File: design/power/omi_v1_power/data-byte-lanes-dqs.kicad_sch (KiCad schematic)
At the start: 3 parts

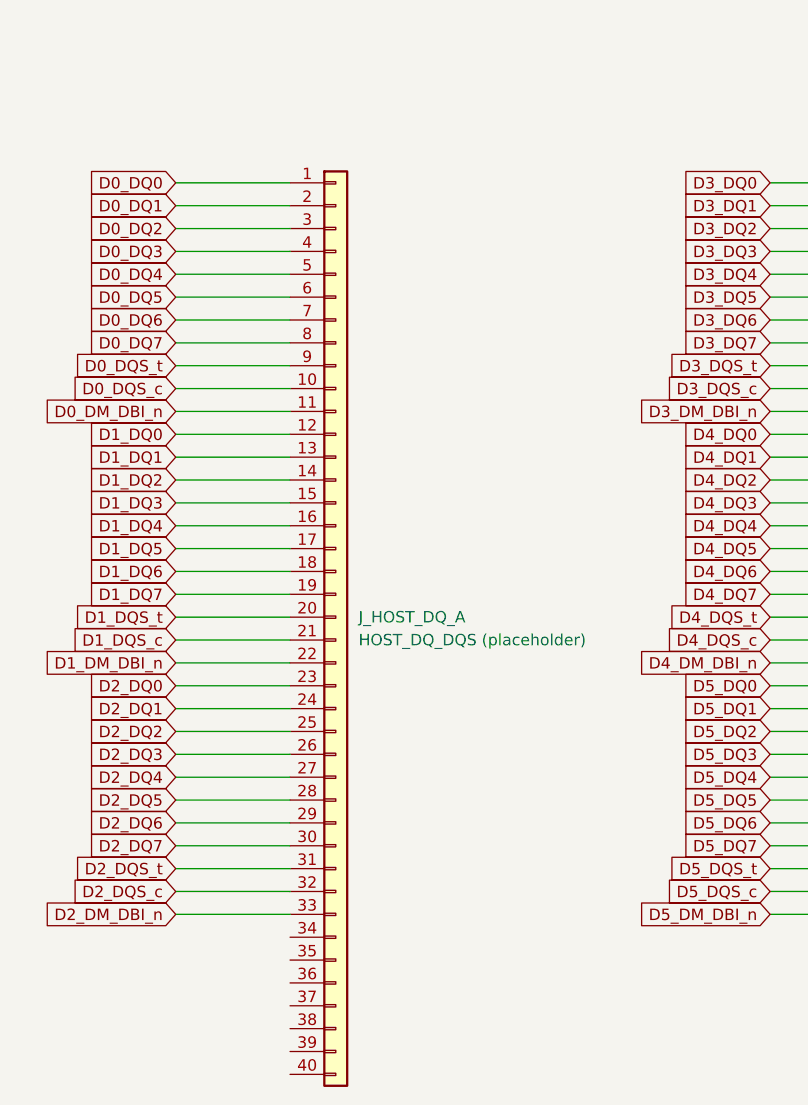
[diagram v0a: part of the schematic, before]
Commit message: feat(phase3): remove redundant J_HOST_DQ_A placeholder (byte lanes D0-D2)
J1 carries every D0/D1/D2 DQ/DQS/DM net; each verified to still hold
{J1, U_DRAMn} after removal (e.g. D0_DQ0 -> {J1, U_DRAM0}). Removed symbol + its
33 pin global labels + 33 wire stubs. J_HOST_DQ_B/C intact (verified: 33/22
labels, nets unchanged). ERC 132 -> 125 (data pin_not_connected 32 -> 25).

Co-Authored-By: Claude Opus 4.8 (1M context) <noreply@anthropic.com>
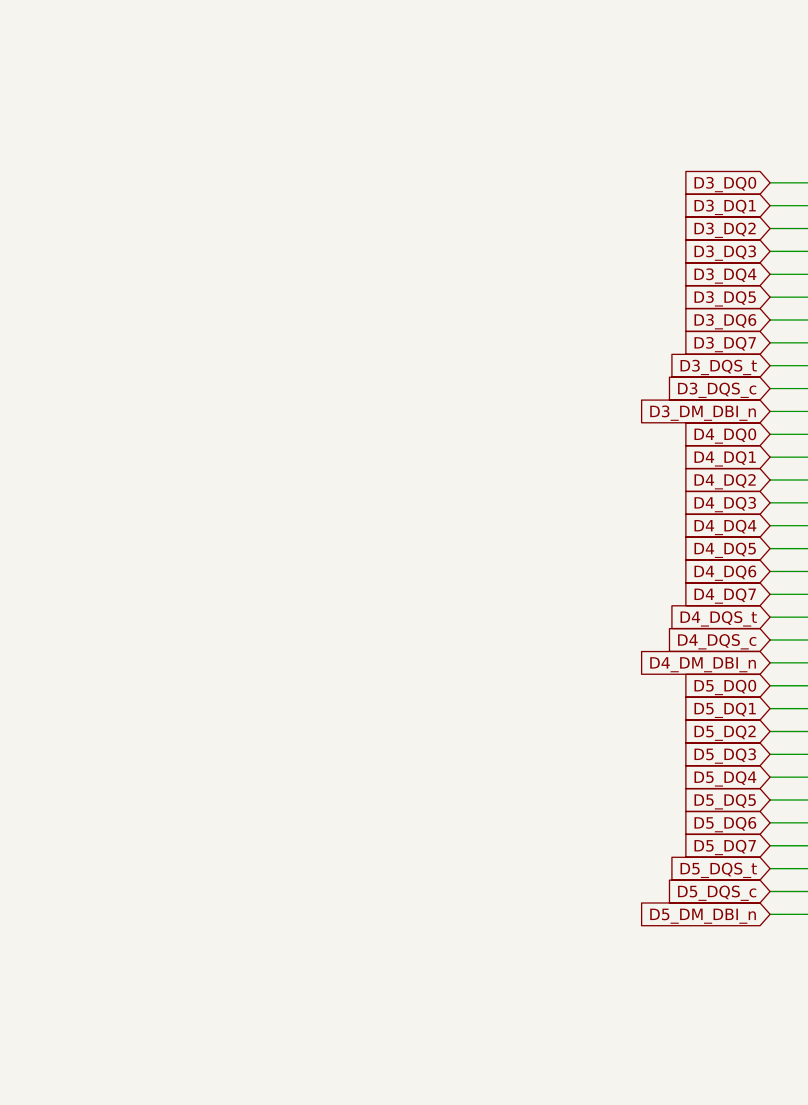
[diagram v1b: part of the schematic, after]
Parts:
- removed J_HOST_DQ_A: HOST_DQ_DQS (placeholder), symbol Connector_Generic:Conn_01x40

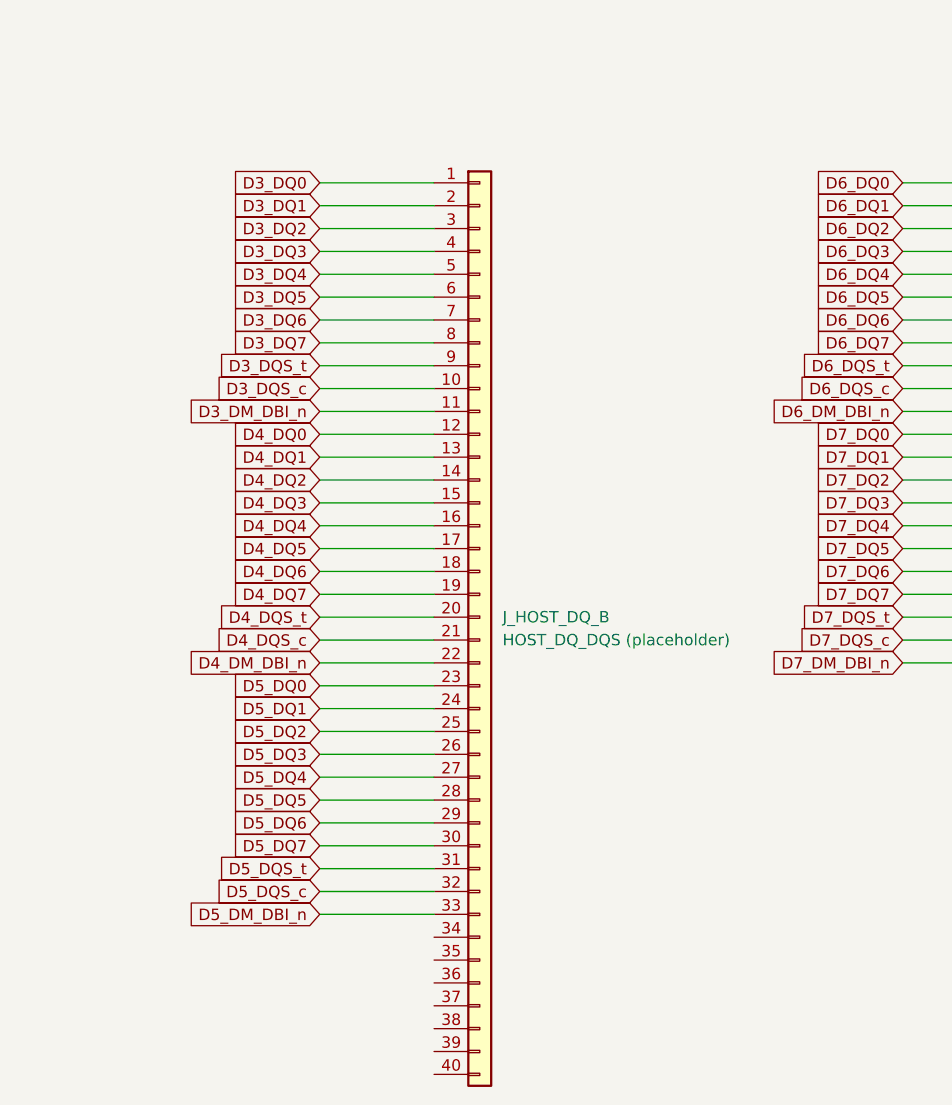
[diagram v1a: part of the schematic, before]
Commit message: feat(phase3): remove redundant J_HOST_DQ_B placeholder (byte lanes D3-D5)
J1 carries every D3/D4/D5 net; D3_DQ0 verified {J1, U_DRAM3} after removal.
Removed symbol + 33 labels + 33 wires. J_HOST_DQ_C intact. ERC 125 -> 118.

Co-Authored-By: Claude Opus 4.8 (1M context) <noreply@anthropic.com>
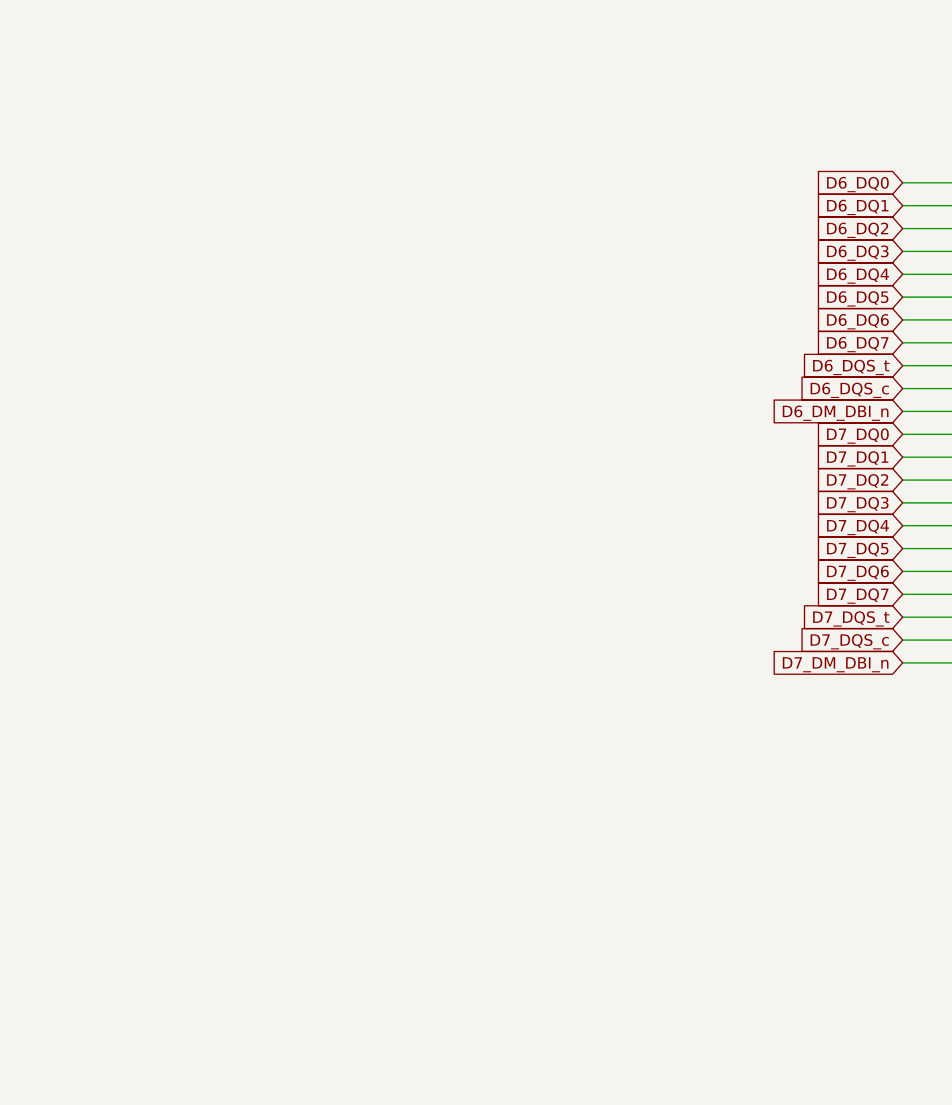
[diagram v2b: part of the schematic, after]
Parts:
- removed J_HOST_DQ_B: HOST_DQ_DQS (placeholder), symbol Connector_Generic:Conn_01x40

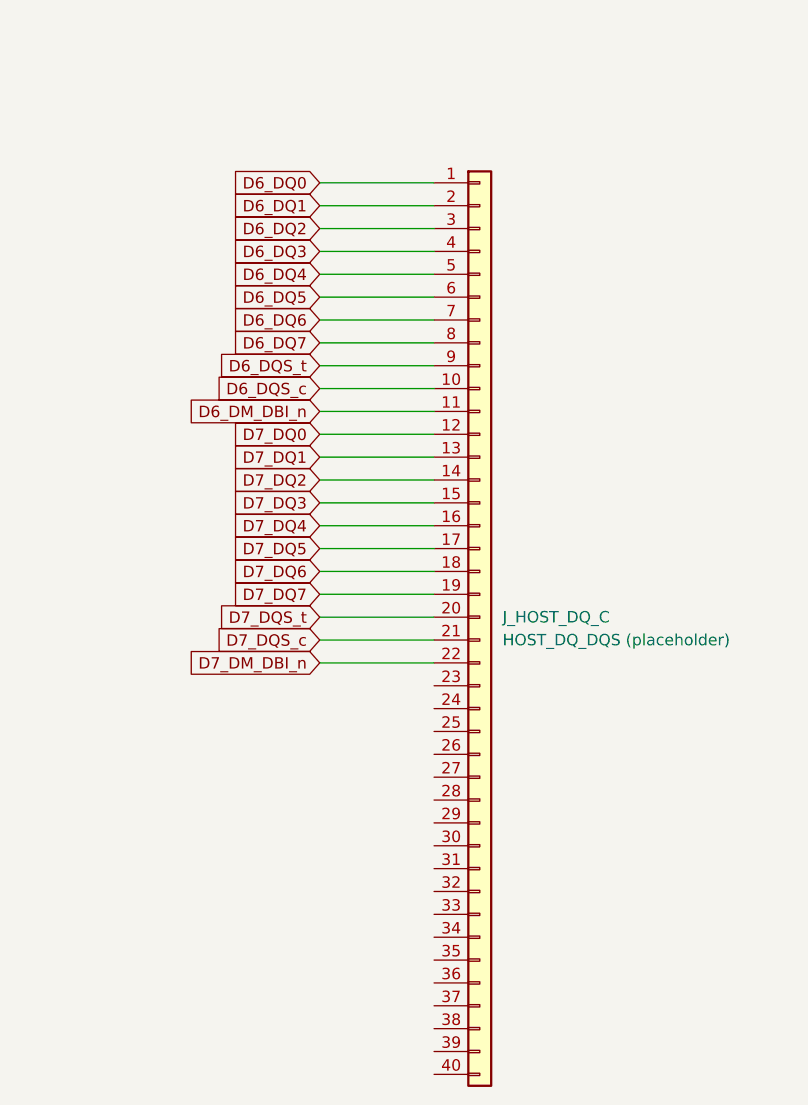
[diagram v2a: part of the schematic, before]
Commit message: feat(phase3): remove redundant J_HOST_DQ_C placeholder (byte lanes D6-D7)
J1 carries every D6/D7 net; D6_DQ0 -> {J1, U_DRAM6}, D7_DQ7 -> {J1, U_DRAM7}
after removal. Removed symbol + 22 labels + 22 wires. The data sheet now holds
only its descriptive text note; DQ/DQS connectivity rides J1 (edge) <-> DRAM
(acc) via global labels. ERC 118 -> 100 (data sheet now 0 violations).

Co-Authored-By: Claude Opus 4.8 (1M context) <noreply@anthropic.com>
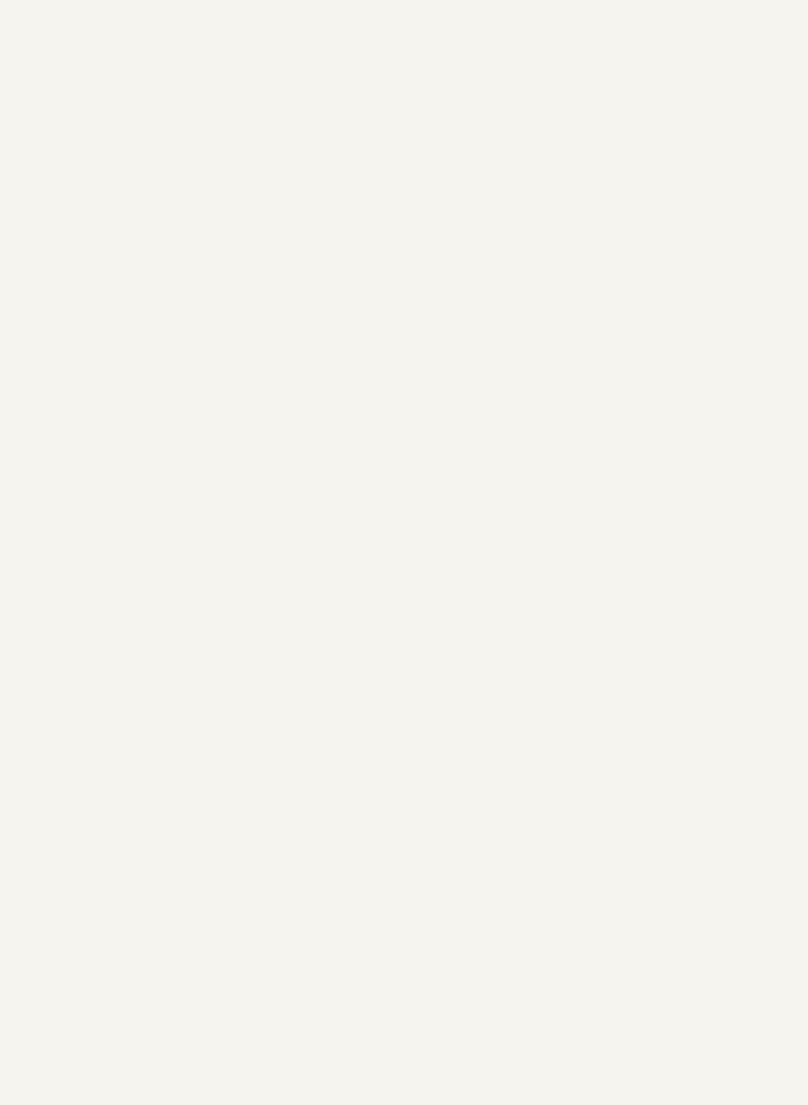
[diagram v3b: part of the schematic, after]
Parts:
- removed J_HOST_DQ_C: HOST_DQ_DQS (placeholder), symbol Connector_Generic:Conn_01x40

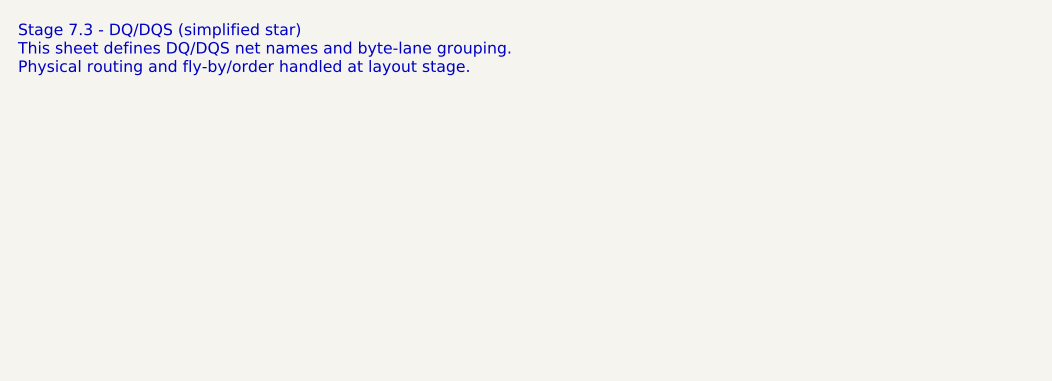
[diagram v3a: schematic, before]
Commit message: polish(schematic): v1.1.0 title blocks + sheet annotations (no electrical change)
Hand-done KiCad 9 GUI pass over all five schematic sheets. Title-block
and text-box content only — no wiring, no component, no net changes.

- Title block (all sheets): Company=OMI, Rev=1.1.0, Date=2026-06-02,
  plus functional per-sheet titles.
- Repurposed the previously-empty DQ/DQS sheet into a byte-lane reference table.
- Added a mechanical caveat text box on the edge (UDIMM) sheet.
- Added a power-rail summary text box on the root sheet.
- omi_v1_power.kicad_prl: project-local UI state saved with the GUI session.

Electrical integrity is asserted to be unchanged and is verified downstream
by the export pipeline (ERC=0 gate + byte-identical netlist and BOM).

Co-Authored-By: Claude Opus 4.8 (1M context) <noreply@anthropic.com>
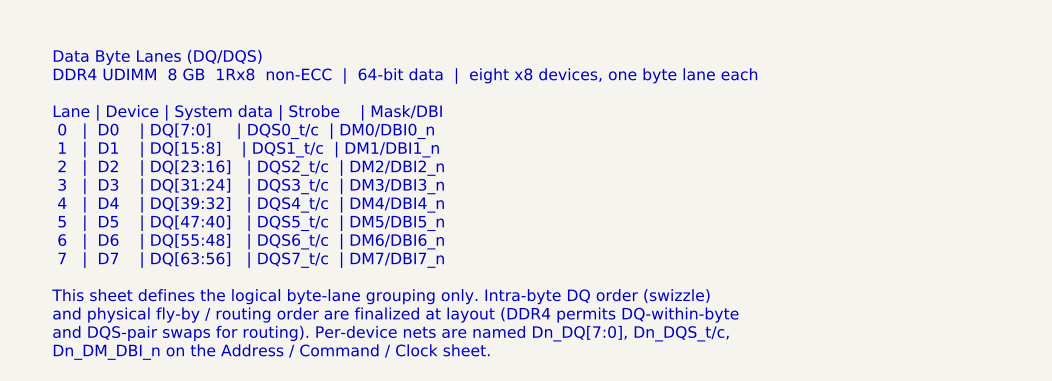
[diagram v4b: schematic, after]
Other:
- note added: "Data Byte Lanes (DQ/DQS) DDR4 UDIMM 8 GB 1Rx8 non-ECC | 64-bit data | eight x8 devices, one byte lane each Lane | Device | System data | Strobe | Mask/DBI 0 | D0 | DQ[7:0] | DQS0_t/c | DM0/DBI0_n 1 | D1 | DQ[15:8] | DQS1_t/c | DM1/DBI1_n 2 | D2 | DQ[23:16] | DQS2_t/c | DM2/DBI2_n 3 | D3 | DQ[31:24] | DQS3_t/c | DM3/DBI3_n 4 | D4 | DQ[39:32] | DQS4_t/c | DM4/DBI4_n 5 | D5 | DQ[47:40] | DQS5_t/c | 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"
- note removed: "Stage 7.3 - DQ/DQS (simplified star) This sheet defines DQ/DQS net names and byte-lane grouping. Physical routing and fly-by/order handled at layout stage."
- company: (none) -> OMI
- title: (none) -> Data Byte Lanes (DQ/DQS)
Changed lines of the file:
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@@
 	(generator_version "9.0")
 	(paper "A4")
-	(text "Stage 7.3 - DQ/DQS (simplified star)\nThis sheet defines DQ/DQS net names and byte-lane grouping.\nPhysical routing and fly-by/order handled at layout stage.\n"
+	(title_block
+		(title "Data Byte Lanes (DQ/DQS)")
+		(date "2026-06-02")
+		(rev "1.1.0")
+		(company "OMI")
+	)
+	(text "Data Byte Lanes (DQ/DQS)\nDDR4 UDIMM  8 GB  1Rx8  non-ECC  |  64-bit data  |  eight x8 devices, one byte lane each\n\nLane | Device | System data | Strobe    | Mask/DBI\n 0   |  D0    | DQ[7:0]     | DQS0_t/c  | DM0/DBI0_n\n 1   |  D1    | DQ[15:8]    | DQS1_t/c  | DM1/DBI1_n\n 2   |  D2    | DQ[23:16]   | DQS2_t/c  | DM2/DBI2_n\n 3   |  D3    | DQ[31:24]   | DQS3_t/c  | DM3/DBI3_n\n 4   |  D4    | DQ[39:32]   | DQS4_t/c  | DM4/DBI4_n\n 5   |  D5    | DQ[47:40]   | DQS5_t/c  | DM5/DBI5_n\n 6   |  D6    | DQ[55:48]   | DQS6_t/c  | DM6/DBI6_n\n 7   |  D7    | DQ[63:56]   | DQS7_t/c  | DM7/DBI7_n\n\nThis sheet defines the logical byte-lane grouping only. Intra-byte DQ order (swizzle)\nand physical fly-by / routing order are finalized at layout (DDR4 permits DQ-within-byte\nand DQS-pair swaps for routing). Per-device nets are named Dn_DQ[7:0], Dn_DQS_t/c,\nDn_DM_DBI_n on the Address / Command / Clock sheet."
 		(exclude_from_sim no)
-		(at 16.256 20.574 0)
+		(at 20.066 37.846 0)
 		(effects
 			(font
